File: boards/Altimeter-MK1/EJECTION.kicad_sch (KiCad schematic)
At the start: 35 parts

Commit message: finished ejection schematic
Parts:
- removed Q? (x6): Q_NMOS_DGS, symbol Device:Q_NMOS_DGS
- added Q1, Q2, Q3, Q4, Q5, Q6: AOD442G, Package_TO_SOT_SMD:TO-252-2, symbol Device:Q_NMOS_GDS
- R1, R13, R17, R21, R6, R9: renamed from R?; value R_US -> 3.3k
- R10, R14, R18, R22, R4, R5: renamed from R?; value R_US -> 1k
- R11, R15, R19, R2, R23, R7: renamed from R?; value R_US -> 100k
- R12, R16, R20, R24, R3, R8: renamed from R?; value R_US -> 27k
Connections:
- net GND2: now also Q1.3 (S), Q2.3 (S), Q3.3 (S), Q4.3 (S), Q5.3 (S), Q6.3 (S)
- net cmp_out_a: now also Q1.1 (G)
- net cmp_out_b: now also Q2.1 (G)
- net cmp_out_c: now also Q3.1 (G)
- net cmp_out_d: now also Q4.1 (G)
- net cmp_out_e: now also Q5.1 (G)
- net cmp_out_f: now also Q6.1 (G)
- net fet_a: now also Q1.2 (D)
- net fet_b: now also Q2.2 (D)
- net fet_c: now also Q3.2 (D)
- net fet_d: now also Q4.2 (D)
- net fet_e: now also Q5.2 (D)
- net fet_f: now also Q6.2 (D)

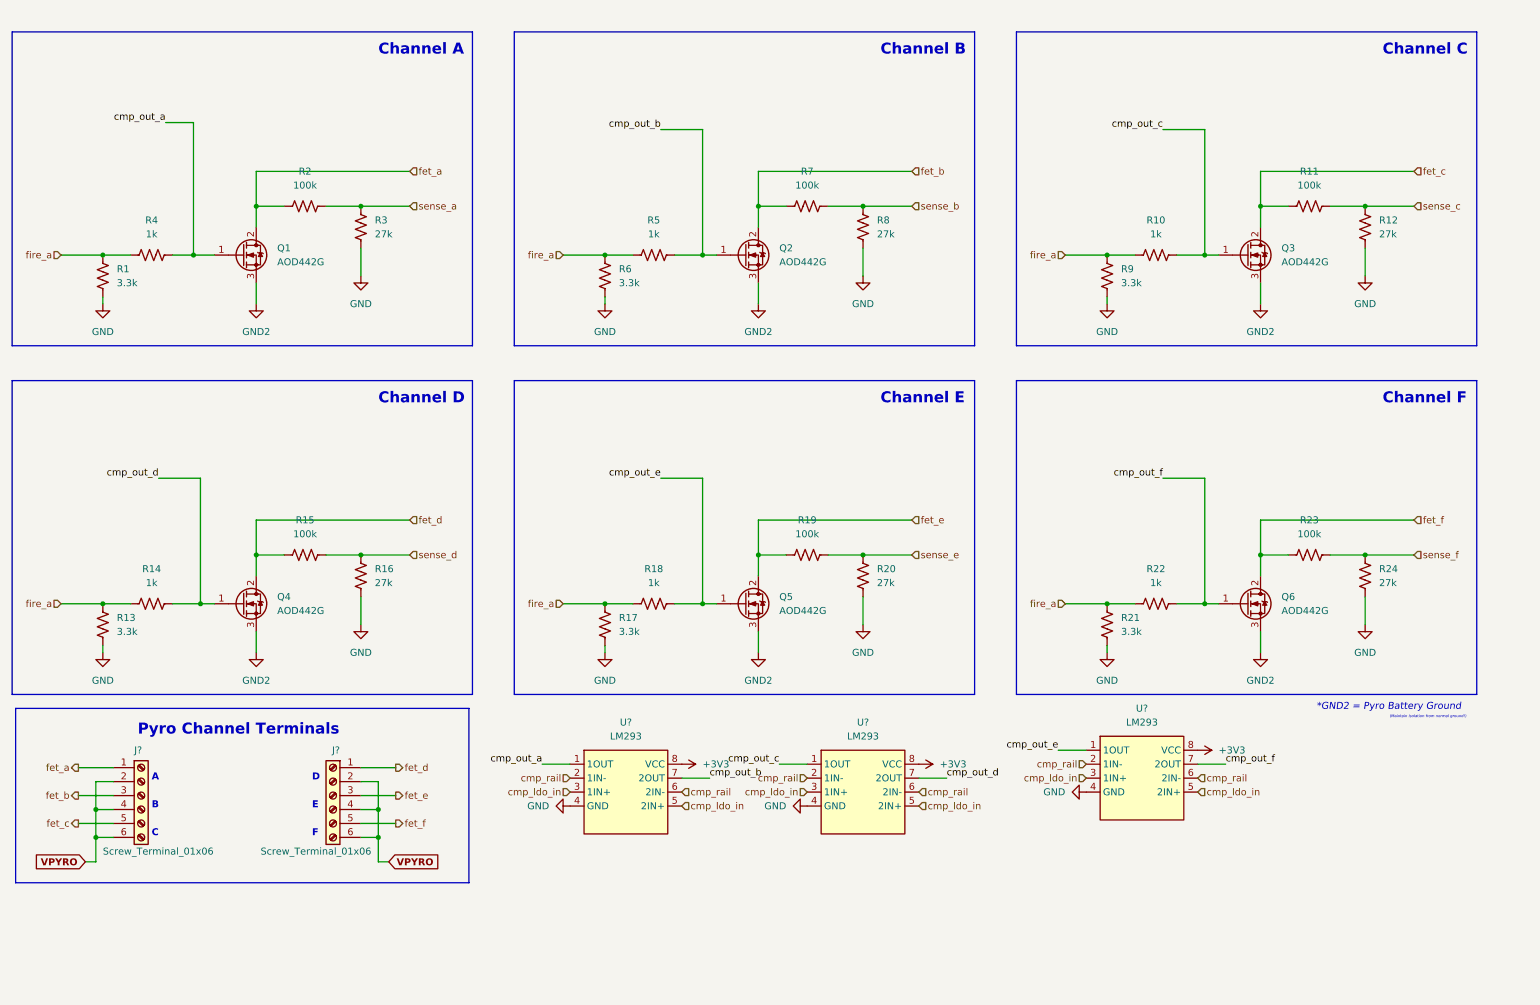
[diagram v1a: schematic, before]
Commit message: Av 688/altimeter igniter schematic (#112)
* No changes just created new branch for ejection

* Made Pyro Channel Screw Terminals

* Replaced 3V3 label with Golbal flag

* added lm293 chip to ejection schematic

* finished ejection schematic

* slight clean up

* more clean up

* Organized Ejection Schematic

Co-authored-by: navyasm <108916984+navyasm@users.noreply.github.com>
Co-authored-by: Peter Giannetos <pg19@illinois.edu>
Co-authored-by: Arna Bhardwaj <arnabhardwaj@Arnas-MacBook-Air.local>
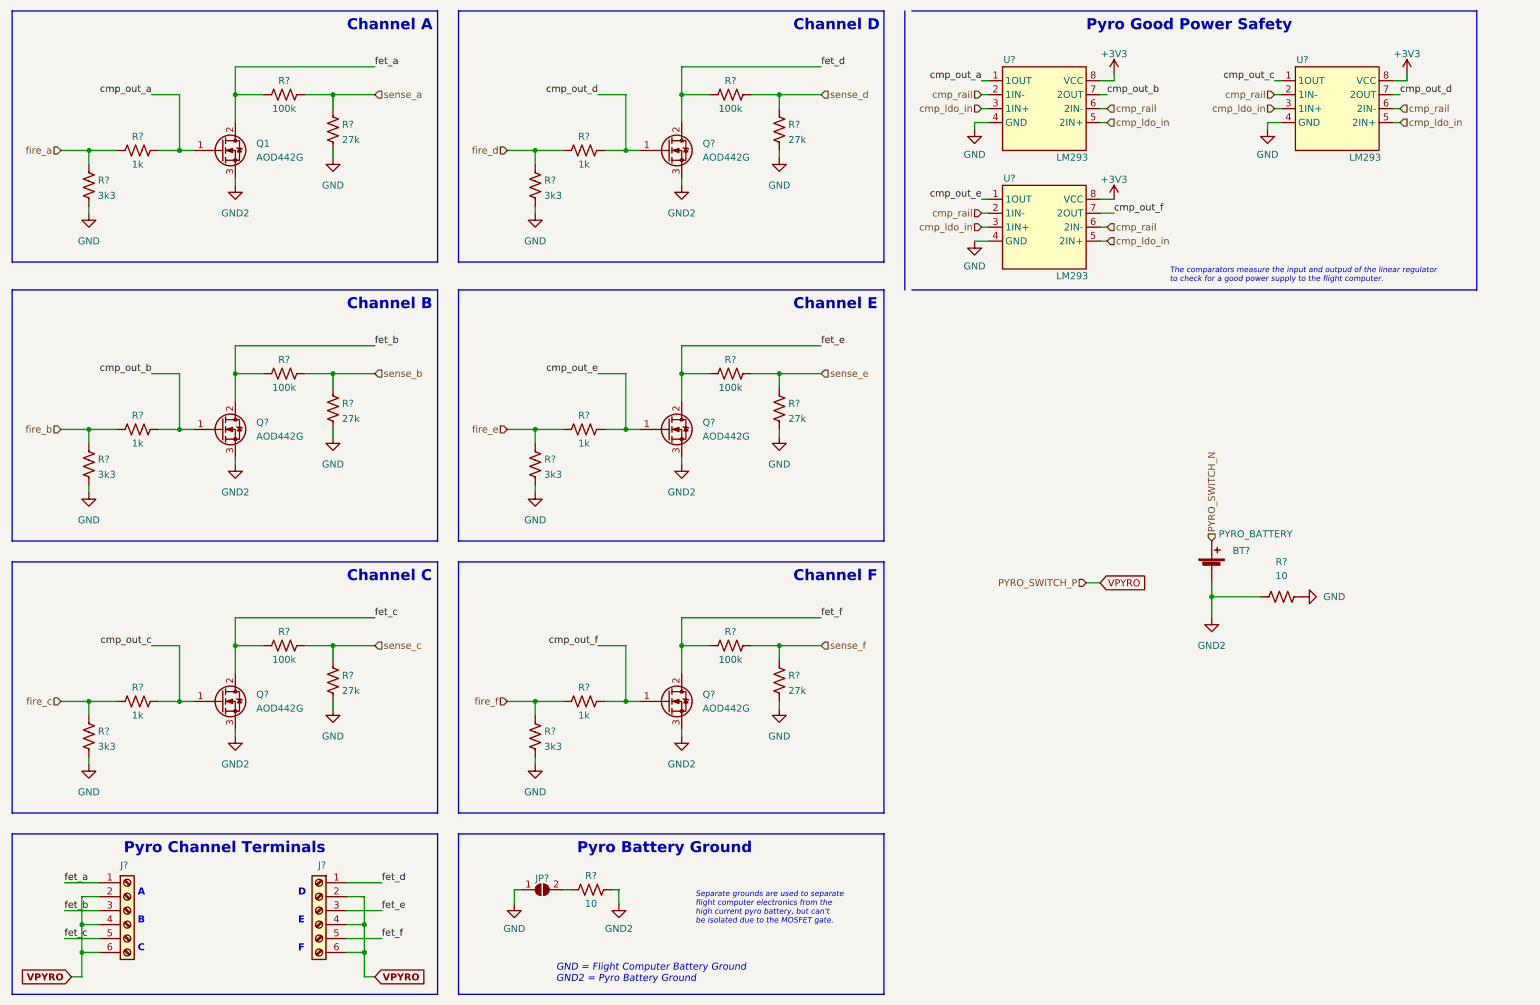
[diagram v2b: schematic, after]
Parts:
- removed Q2, Q3, Q4, Q5, Q6: AOD442G, Package_TO_SOT_SMD:TO-252-2, symbol Device:Q_NMOS_GDS
- removed R10, R14, R18, R22, R5: 1k, symbol Device:R_US
- removed R11, R15, R19, R23, R7: 100k, symbol Device:R_US
- removed R12, R16, R20, R24, R8: 27k, symbol Device:R_US
- removed R13, R17, R21, R6, R9: 3.3k, symbol Device:R_US
- added BT?: PYRO_BATTERY, symbol Device:Battery_Cell
- added JP?: SolderJumper_2_Open, symbol Jumper:SolderJumper_2_Open
- added Q? (x5): AOD442G, Package_TO_SOT_SMD:TO-252-2, symbol Device:Q_NMOS_GDS
- added R? (x5): 3k3, symbol Device:R_US
- added R? (x5): 1k, symbol Device:R_US
- added R? (x5): 27k, symbol Device:R_US
- added R? (x5): 100k, symbol Device:R_US
- added R? (x2): 10, symbol Device:R_US
- R?: renamed from R1; value 3.3k -> 3k3
- renumbered R2 to R?, R3 to R?, R4 to R?
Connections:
- net GND: now also JP?.1 (A), R?.2, R?.2, R?.2, R?.2, R?.2, R?.2, R?.2, R?.2, R?.2, R?.2, R?.2
- net GND2: now also BT?.2 (-), Q?.3 (S), Q?.3 (S), Q?.3 (S), Q?.3 (S), Q?.3 (S), R?.1, R?.2
- net cmp_out_b: now also Q?.1 (G), R?.2
- net cmp_out_c: now also Q?.1 (G), R?.2
- net cmp_out_d: now also Q?.1 (G), R?.2
- net cmp_out_e: now also Q?.1 (G), R?.2
- net cmp_out_f: now also Q?.1 (G), R?.2
- net fet_b: now also Q?.2 (D), R?.1
- net fet_c: now also Q?.2 (D), R?.1
- net fet_d: now also Q?.2 (D), R?.1
- net fet_e: now also Q?.2 (D), R?.1
- net fet_f: now also Q?.2 (D), R?.1
- net sense_b: now also R?.1, R?.2
- net sense_c: now also R?.1, R?.2
- net sense_d: now also R?.1, R?.2
- net sense_e: now also R?.1, R?.2
- net sense_f: now also R?.1, R?.2
- new net: JP?.2 (B), R?.1
- new net PYRO_SWITCH_N: BT?.1 (+)
- new net fire_b: R?.1, R?.1
- new net fire_c: R?.1, R?.1
- new net fire_d: R?.1, R?.1
- new net fire_e: R?.1, R?.1
- new net fire_f: R?.1, R?.1
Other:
- note added: "GND = Flight Computer Battery Ground GND2 = Pyro Battery Ground"
- note added: "Pyro Battery Ground"
- note added: "Pyro Good Power Safety"
- note added: "Separate grounds are used to separate flight computer electronics from the high current pyro battery, but can't be isolated due to the MOSFET gate."
- note added: "The comparators measure the input and outpud of the linear regulator to check for a good power supply to the flight computer."
- note removed: "(Maintain isolation from normal ground!)"
- note removed: "*GND2 = Pyro Battery Ground"
- moved on the sheet: J?, Q1, R?, U?

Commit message: Organized schematic
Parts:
- removed JP?: SolderJumper_2_Open, symbol Jumper:SolderJumper_2_Open
- removed R?: 10, symbol Device:R_US
- added J?: Screw_Terminal_01x02, symbol Connector:Screw_Terminal_01x02
- R?: value 100k -> R_US
- R?: value 27k -> R_US
- R?: value 3k3 -> R_US
- R?: value 1k -> R_US
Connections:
- net VPYRO: now also J?.1 (Pin_1)
- net PYRO_SWITCH_N renamed Pyro_SWT_P
- net Pyro_SWT_P: now also J?.2 (Pin_2)
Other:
- note added: "Pyro Battery"
- note added: "Pyro Screw Terminals"
- note removed: "Pyro Battery Ground"
- note removed: "Pyro Channel Terminals"
- note removed: "Separate grounds are used to separate flight computer electronics from the high current pyro battery, but can't be isolated due to the MOSFET gate."
- moved on the sheet: BT?, J?, R?

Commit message: igniters cleanup
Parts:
- BT?: value PYRO_BATTERY -> (none)
- J? (x2): value Screw_Terminal_01x06 -> (none)
- J?: value Screw_Terminal_01x02 -> (none)
- Q1, Q? (x5): value AOD442G -> (none); footprint Package_TO_SOT_SMD:TO-252-2 -> (none)
- R? (x5): value 3k3 -> (none)
- R? (x5): value 1k -> (none)
- R? (x5): value 27k -> (none)
- R? (x5): value 100k -> (none)
- R?: value 10 -> (none)
- U? (x3): value LM293 -> (none)
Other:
- moved on the sheet: BT?, J?, R?

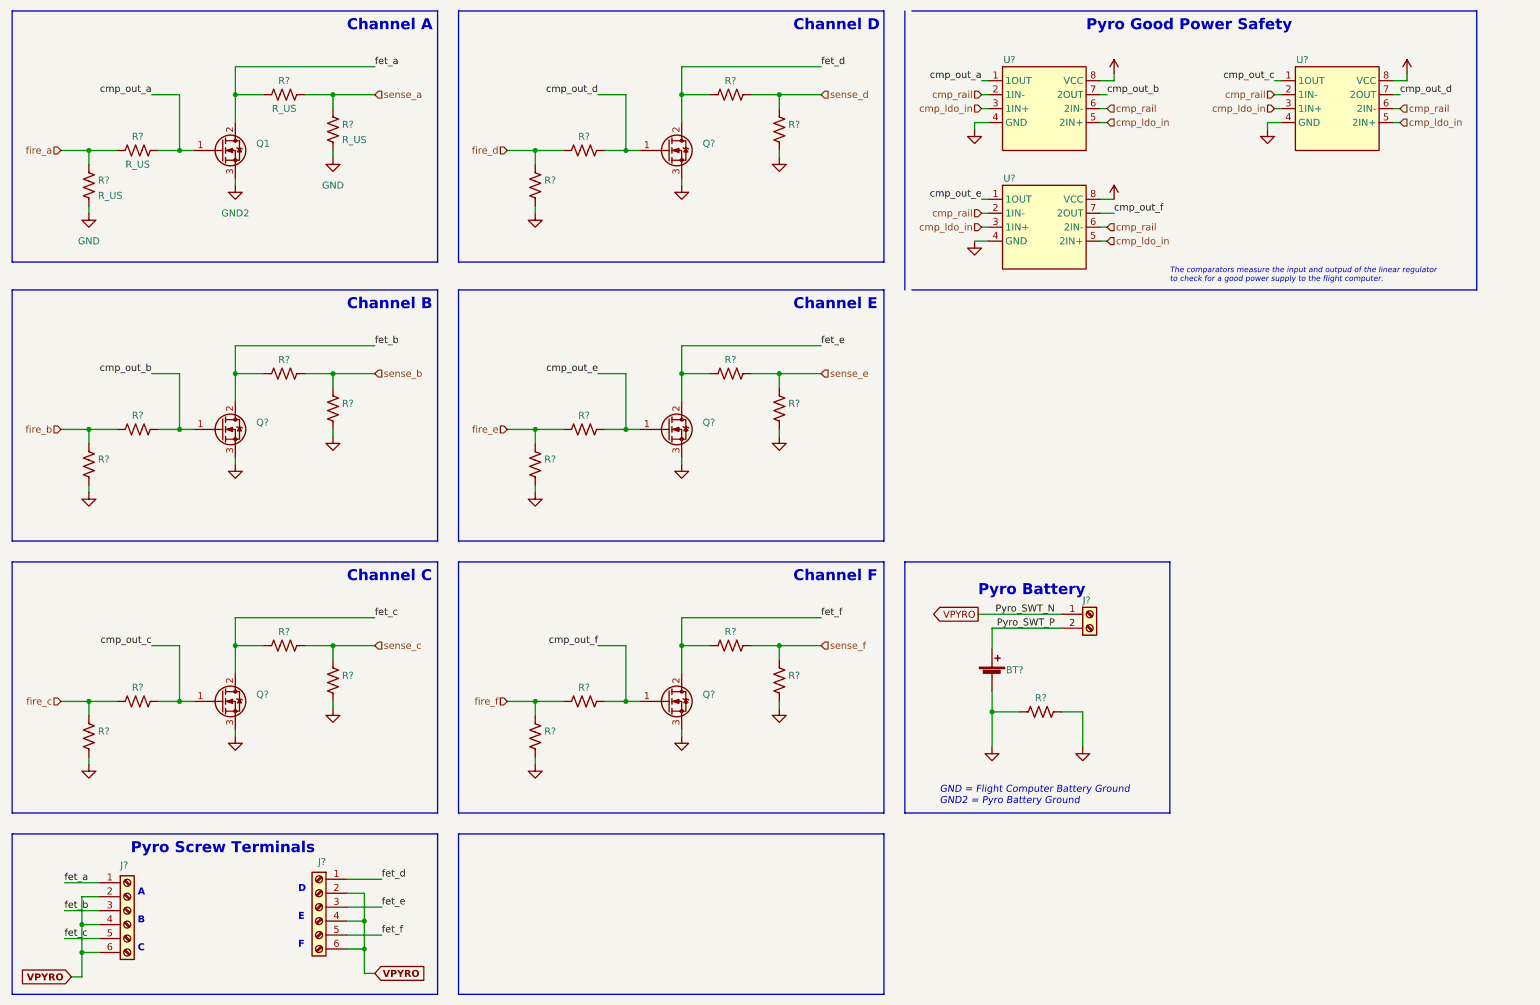
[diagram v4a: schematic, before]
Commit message: added footprints to resistors
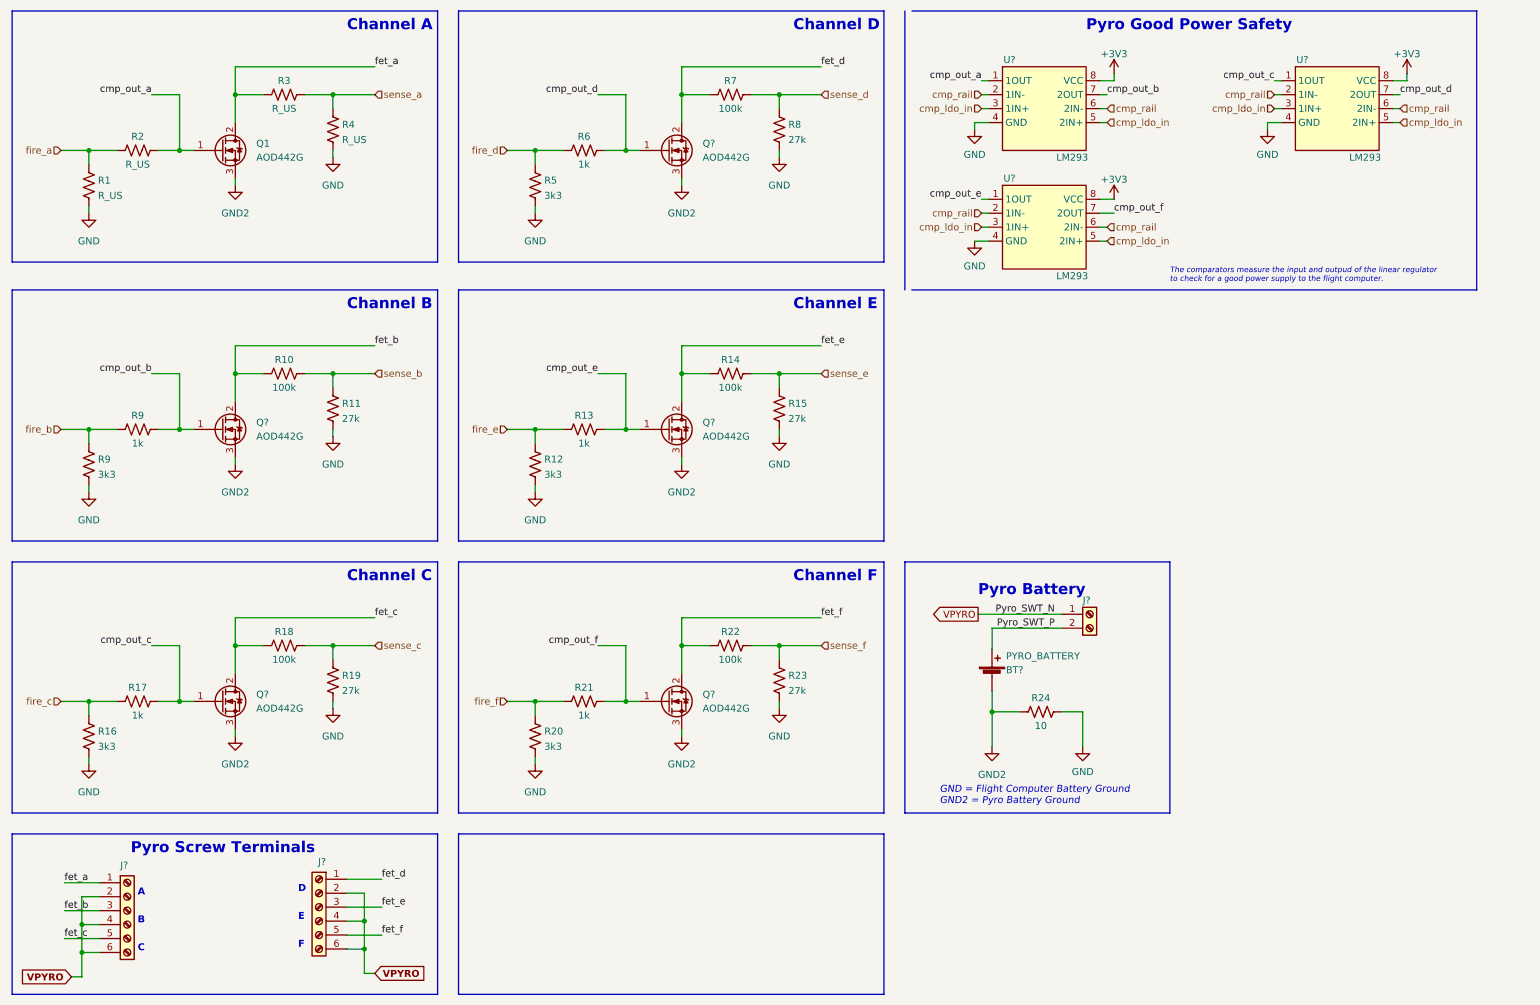
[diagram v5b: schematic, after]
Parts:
- BT?: value (none) -> PYRO_BATTERY
- J? (x2): value (none) -> Screw_Terminal_01x06
- J?: value (none) -> ~
- Q1, Q? (x5): value (none) -> AOD442G; footprint (none) -> Package_TO_SOT_SMD:TO-252-2
- R1, R2, R3, R4: renamed from R?; footprint (none) -> Resistor_SMD:R_01005_0402Metric
- R10, R14, R18, R22, R7: renamed from R?; value (none) -> 100k; footprint (none) -> Resistor_SMD:R_01005_0402Metric
- R11, R15, R19, R23, R8: renamed from R?; value (none) -> 27k; footprint (none) -> Resistor_SMD:R_01005_0402Metric
- R12, R16, R20, R5, R9: renamed from R?; value (none) -> 3k3; footprint (none) -> Resistor_SMD:R_01005_0402Metric
- R13, R17, R21, R6, R9: renamed from R?; value (none) -> 1k; footprint (none) -> Resistor_SMD:R_01005_0402Metric
- R24: renamed from R?; value (none) -> 10; footprint (none) -> Resistor_SMD:R_01005_0402Metric
- U? (x3): value (none) -> LM293
